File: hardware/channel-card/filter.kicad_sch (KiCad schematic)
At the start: 101 parts, among them J181 CUTOFF CV (1 V/oct), SW181 FILTER BYPASS (latching), U101 SSI2144, U102 SSI2144, U103 LM13700, U104 NE5532, U105 NE5532, U106 NE5532, U107 NE5532, U108 DG413DY

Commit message: Redraw filter and input sheets with wires; low-cut to 100 Hz
Filter and Input sheets are now drawn with real wires inside each
circuit block, generated by filter_wired.py and input_wired.py and
checked pin by pin against reference netlists (the Input reference is
frozen in scripts/reference). SSI2144 symbol rearranged so the ladder
capacitors sit beside their pins. Obsolete label-only post scripts
removed. The input low-cut moves to 100 Hz with 24k/47k resistors
(decision 73).

Co-Authored-By: Claude Opus 5.5 <noreply@anthropic.com>
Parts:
- J181: value CUTOFF CV (1 V/oct) -> CUTOFF CV 1 V/oct
- JP101, JP151: value DRIVE (fit both = MEDIUM) -> DRIVE: fit both = MEDIUM
- JP102, JP152: value Q COMP (1-2 HALF, 2-3 FULL, open NONE) -> Q COMP: 1-2 HALF, 2-3 FULL; Note (none) -> Open = no bass compensation
- RV101, RV151: value 50k (CUTOFF OFFSET) -> 50k CUTOFF OFFSET
- RV181: value 50k lin (CUTOFF) -> 50k lin CUTOFF
- RV182: value 50k (V/OCT) -> 50k V/OCT
- RV183: value 10k rev. audio (RESONANCE) -> 10k rev. audio RESONANCE
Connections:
- net AGND: now also R106.1, R116.1, R156.1, R166.1, R186.1; no longer R106.2, R116.2, R156.2, R166.2, R186.2
- net BYP: now also R186.2; no longer R186.1
- net QW: now also R120.2, R170.2; no longer R120.1, R170.1
- net BYP_LED: no longer names the net of D183.2 (A), R185.2
- net BYP_LEDK: no longer names the net of D183.1 (K), SW181.4 (A)
- net CUTW: no longer names the net of R181.1, RV181.2
- net CVIN: no longer names the net of J181.T, R182.1
- net FSUM: no longer names the net of C181.1, R181.2, R182.2, R183.1, U107.2 (-)
- net FVO: no longer names the net of R183.2, RV182.1
- net L_C1A: no longer names the net of C102.1, U101.13 (C1A)
- net L_C1B: no longer names the net of C102.2, U101.12 (C1B)
- net L_C2A: no longer names the net of C103.1, U101.11 (C2A)
- net L_C2B: no longer names the net of C103.2, U101.10 (C2B)
- net L_C3A: no longer names the net of C104.1, U101.6 (C3A)
- net L_C3B: no longer names the net of C104.2, U101.7 (C3B)
- net L_C4A: no longer names the net of C105.1, U101.4 (C4A)
- net L_C4B: no longer names the net of C105.2, U101.5 (C4B)
- net L_DRVA: no longer names the net of JP101.1 (Pin_1), R103.2
- net L_FC: no longer names the net of R108.1, R109.1, R110.2, U101.15 (FREQ_CTRL)
- net L_FILT: no longer names the net of R113.2, U106.1, U108.14
- net L_FIN: no longer names the net of JP101.2 (Pin_2), R102.2, R104.1, R119.1, U104.1
- net L_FIN: now also R118.2; no longer R118.1
- net L_IABC: no longer names the net of U103.1
- net L_IABC: now also R120.1; no longer R120.2
- net L_OFS: no longer names the net of R109.2, RV101.2
- net L_OUTI: no longer names the net of C106.1, R111.1, U101.3 (OUT), U105.2 (-)
- net L_PA: no longer names the net of C107.2, R112.1, U106.3 (+)
- net L_PFB: no longer names the net of R113.1, R114.1, U106.2 (-)
- net L_PSUM: no longer names the net of R101.2, R102.1, R103.1, U104.2 (-)
- net L_QP: no longer names the net of R107.1, U101.14 (Q_CTRL)
- net L_QPLUS: no longer names the net of R115.1, U103.3 (+)
- net L_QSUM: no longer names the net of JP102.2 (Pin_2), R117.2, U103.4 (-)
- net L_QSUM: now also R116.2; no longer R116.1
- net L_RFULL: no longer names the net of JP102.3 (Pin_3), R119.2
- net L_RHALF: no longer names the net of JP102.1 (Pin_1)
- net L_RHALF: now also R118.1; no longer R118.2
- net L_SIN: no longer names the net of R104.2, R105.1, U101.1 (SIG_IN+)
- net L_SINN: no longer names the net of U101.2 (SIG_IN-), U103.5
- net L_SINN: now also R106.2; no longer R106.1
- net QBOT: no longer names the net of D181.2 (A), RV183.1
- net QMID: no longer names the net of D181.1 (K), D182.2 (A)
- net QTOP: no longer names the net of R184.2, RV183.3
- net R_C1A: no longer names the net of C152.1, U102.13 (C1A)
- net R_C1B: no longer names the net of C152.2, U102.12 (C1B)
- net R_C2A: no longer names the net of C153.1, U102.11 (C2A)
- net R_C2B: no longer names the net of C153.2, U102.10 (C2B)
- net R_C3A: no longer names the net of C154.1, U102.6 (C3A)
- net R_C3B: no longer names the net of C154.2, U102.7 (C3B)
- net R_C4A: no longer names the net of C155.1, U102.4 (C4A)
- net R_C4B: no longer names the net of C155.2, U102.5 (C4B)
- net R_DRVA: no longer names the net of JP151.1 (Pin_1), R153.2
- net R_FC: no longer names the net of R158.1, R159.1, R160.2, U102.15 (FREQ_CTRL)
- net R_FILT: no longer names the net of R163.2, U106.7, U108.11
- net R_FIN: no longer names the net of JP151.2 (Pin_2), R152.2, R154.1, R169.1, U104.7
- net R_FIN: now also R168.2; no longer R168.1
- net R_IABC: no longer names the net of U103.16
- net R_IABC: now also R170.1; no longer R170.2
- net R_OFS: no longer names the net of R159.2, RV151.2
- net R_OUTI: no longer names the net of C156.1, R161.1, U102.3 (OUT), U105.6 (-)
- net R_PA: no longer names the net of C157.2, R162.1, U106.5 (+)
- net R_PFB: no longer names the net of R163.1, R164.1, U106.6 (-)
- net R_PSUM: no longer names the net of R151.2, R152.1, R153.1, U104.6 (-)
- net R_QP: no longer names the net of R157.1, U102.14 (Q_CTRL)
- net R_QPLUS: no longer names the net of R165.1, U103.14 (+)
- net R_QSUM: no longer names the net of JP152.2 (Pin_2), R167.2, U103.13 (-)
- net R_QSUM: now also R166.2; no longer R166.1
- net R_RFULL: no longer names the net of JP152.3 (Pin_3), R169.2
- net R_RHALF: no longer names the net of JP152.1 (Pin_1)
- net R_RHALF: now also R168.1; no longer R168.2
- net R_SIN: no longer names the net of R154.2, R155.1, U102.1 (SIG_IN+)
- net R_SINN: no longer names the net of U102.2 (SIG_IN-), U103.12
- net R_SINN: now also R156.2; no longer R156.1
- net SPARE_OA: no longer names the net of U107.6 (-), U107.7

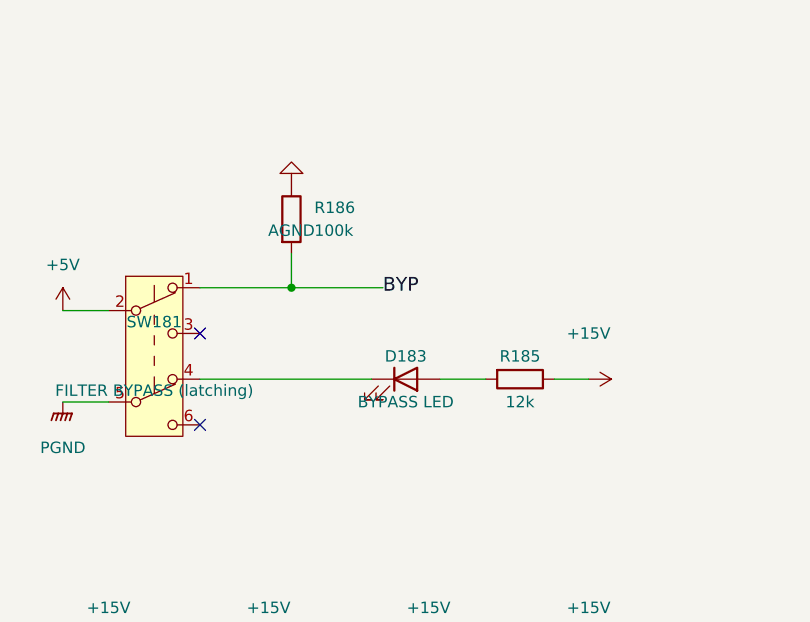
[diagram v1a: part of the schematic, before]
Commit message: Choose GPBS850N latching buttons with printed light caps
Buttons are CW Industries GPBS850N latching DPDT switches (Electrokit)
with 0805 LEDs lighting 3D-printed translucent caps (decision 75).
The datasheet shows pins 2-3 and 5-6 close when pressed, so every
button now uses pin 3 for logic and pin 6 for the LED. Adds the switch
footprint library, rebuild_all.sh, the state-retention requirement for
the momentary-button backlog item, and ten switches to the second
Electrokit order.

Co-Authored-By: Claude Opus 5.5 <noreply@anthropic.com>
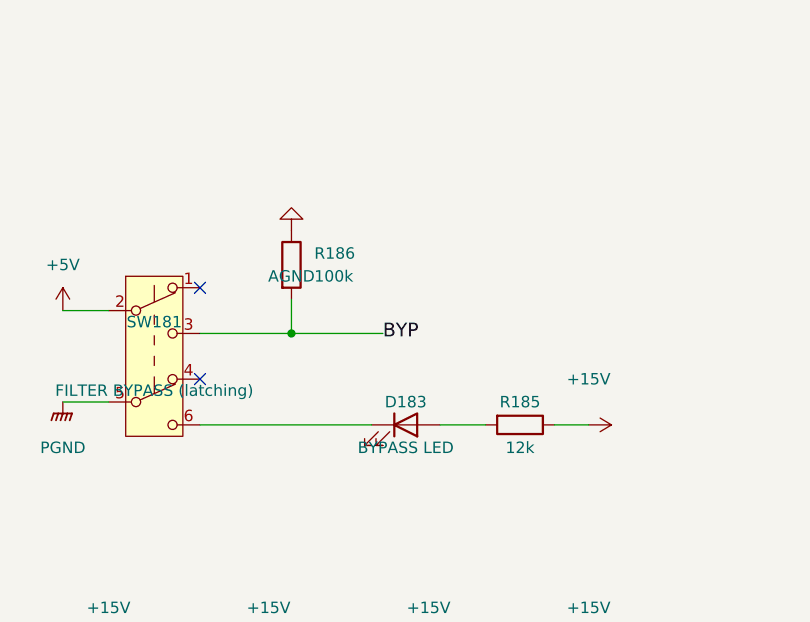
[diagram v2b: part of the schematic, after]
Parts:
- D183: footprint LED_THT:LED_D3.0mm -> LED_SMD:LED_0805_2012Metric
- SW181: footprint (none) -> syntsamix:SW_Latching_8.5x8.5mm_CW_GPBS850N; MPN (none) -> GPBS850N; Manufacturer (none) -> CW Industries; Supplier (none) -> Electrokit; SupplierPN (none) -> 41012905
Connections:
- net BYP: now also SW181.3 (C); no longer SW181.1 (A)
- net at SW181.4 (A): no longer D183.1 (K)
- net at SW181.6 (C): now also D183.1 (K)

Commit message: Add test pads to the channel card sheets
24 bare 1.5 mm test pads on key audio, control and ground nets across
the Input, Filter, Level, Routing and Meter sheets, named by net and
kept out of the BOM (decision 77). Each pad is in the reference
netlists, so the checks prove it sits on the intended net.

Co-Authored-By: Claude Opus 5.5 <noreply@anthropic.com>
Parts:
- added TP101: L_SIN, TestPoint:TestPoint_Pad_D1.5mm, symbol Connector:TestPoint
- added TP102: L_IV, TestPoint:TestPoint_Pad_D1.5mm, symbol Connector:TestPoint
- added TP103: L_POSTFILT, TestPoint:TestPoint_Pad_D1.5mm, symbol Connector:TestPoint
- added TP151: R_SIN, TestPoint:TestPoint_Pad_D1.5mm, symbol Connector:TestPoint
- added TP152: R_IV, TestPoint:TestPoint_Pad_D1.5mm, symbol Connector:TestPoint
- added TP153: R_POSTFILT, TestPoint:TestPoint_Pad_D1.5mm, symbol Connector:TestPoint
- added TP181: FCV, TestPoint:TestPoint_Pad_D1.5mm, symbol Connector:TestPoint
- added TP182: QW, TestPoint:TestPoint_Pad_D1.5mm, symbol Connector:TestPoint
- added TP183: AGND, TestPoint:TestPoint_Pad_D1.5mm, symbol Connector:TestPoint
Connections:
- net AGND: now also TP183.1
- net FCV: now also TP181.1
- net L_IV: now also TP102.1
- net L_POSTFILT: now also TP103.1
- net QW: now also TP182.1
- net R_IV: now also TP152.1
- net R_POSTFILT: now also TP153.1
- net at R154.2, R155.1, U102.1 (SIG_IN+): now also TP151.1
- net at R104.2, R105.1, U101.1 (SIG_IN+): now also TP101.1

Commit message: Check parts against LCSC stock and use basic resistor values
tools/lcsc_check.py checks docs/parts.csv against the JLCPCB/LCSC
catalogue and writes docs/lcsc-check.csv. Non-critical resistors move
to JLC basic values to cut setup fees (decision 79): bus resistors 22k,
VCA input network 100R, cutoff offset 470k, regulator dividers 200R/2k2
(15.1 V). All sheets rebuilt and verified (ERC 0/0).

Co-Authored-By: Claude Opus 5.5 <noreply@anthropic.com>
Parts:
- R109, R159: value 499k -> 470k; ProjectPN SX-R-020 -> SX-R-048

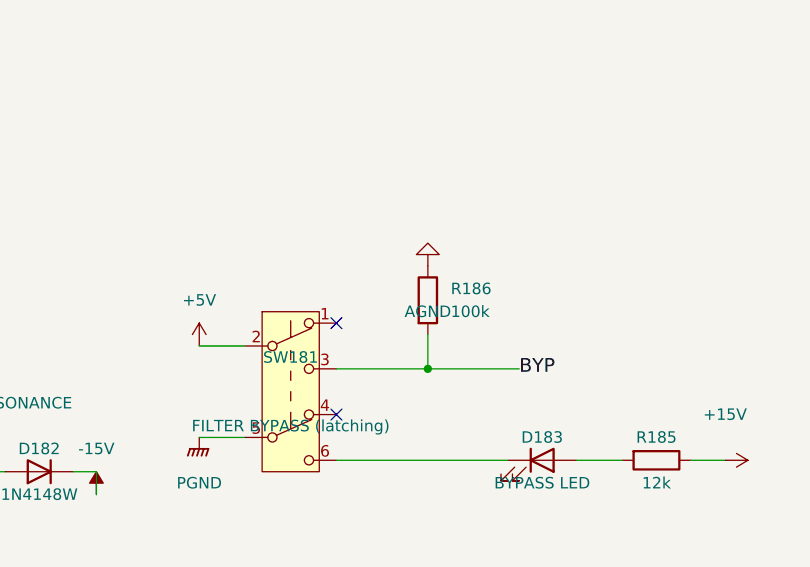
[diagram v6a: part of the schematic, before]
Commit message: Channel card: draw decisions 97 and 98, fader buffer on an OPA2171 (decision 102)
- Level: SC_ENV into the summer's virtual earth through R217 30k1, R218 removed,
  summer + input on AGND (decision 97)
- Q301 emitter and button pull-downs R17, R186, R220, R222, R313, R315, R317 to PGND (decision 98)
- U204 = OPA2171 for the fader buffer and control summer (input range includes V-);
  superdiodes moved to the TL072 U205 (decision 102)
- simulation/level: fader law within 1.2 dB, ducking 10.07 dB per -1 V at every fader position
- Power budget, parts list, STATUS, breadboard test 10 and working notes updated

Co-Authored-By: Claude Opus 5.5 <noreply@anthropic.com>
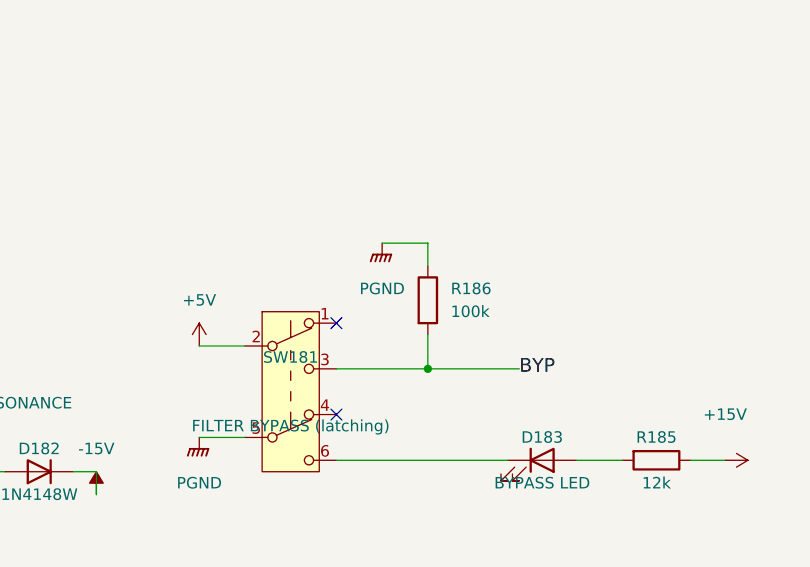
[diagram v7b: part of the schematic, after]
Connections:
- net AGND: no longer R186.1
- net PGND: now also R186.1

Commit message: Channel card: mechanical parts, decisions 110-117
- 110 LM317/LM337 in D2PAK on copper (onsemi, LCSC)
- 111 SMD electrolytics <= 5.4 mm (ROQANG, Panasonic bipolar)
- 112 trimmers and jumper headers on the underside, bottom cover for /system
- 113 low-cut caps C0G 1206
- 114 pot shaft standard T18 15 mm; 115 trim stage scaled to 100k, pots chosen
  (blocked until RoHS declarations)
- 116 RoHS strict for every part and board (process)
- 117 button LED colours (JLCPCB basic 0805), Wurth chain headers
- J181 drawn as Thonkiconn 3.5 mm (pending /system), fields and footprints set,
  five sheets rebuilt, netlists match, ERC 0/0
- STATUS: seven For /system items (CV jack, 0805 meter bezel, panel screws,
  bottom cover, underside keep-out, RoHS invariant, contract doc updates)

Co-Authored-By: Claude Opus 5.5 <noreply@anthropic.com>
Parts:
- C101, C107, C151, C157: footprint Capacitor_THT:C_Radial_D5.0mm_H11.0mm_P2.00mm -> Capacitor_SMD:C_Elec_6.3x5.4; MPN (none) -> EEE-1VA100NP; Manufacturer (none) -> Panasonic; ProjectPN SX-C-003 -> SX-C-023; Supplier (none) -> Mouser; SupplierPN (none) -> 667-EEE-1VA100NP
- D183: MPN (none) -> KT-0805W; Manufacturer (none) -> Hubei KENTO; ProjectPN SX-D-002 -> SX-D-017; Supplier (none) -> LCSC; SupplierPN (none) -> C34499
- J181: footprint (none) -> Connector_Audio:Jack_3.5mm_QingPu_WQP-PJ398SM_Vertical_CircularHoles; MPN (none) -> PJ398SM; Manufacturer (none) -> Qingpu; Note 6.3 mm mono switched jack on the top panel; part and footpr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 -> 3.5 mm Thonkiconn on the top panel with a 1 mm M6 washer (S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; ProjectPN SX-CONN-003 -> SX-CONN-014; Supplier (none) -> Thonk
- RV181: Manufacturer (none) -> Alpha; Supplier (none) -> Thonk
- RV183: MPN (none) -> RD901F-40-15K-C10K; Manufacturer (none) -> Alpha; Note Reverse-audio (C) taper per SSI2144 datasheet Figure 3; par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 -> Reverse-audio (C) taper per SSI2144 datasheet Figure 3; ProjectPN SX-POT-004 -> SX-POT-012; Supplier (none) -> Tayda; SupplierPN (none) -> A-5369
